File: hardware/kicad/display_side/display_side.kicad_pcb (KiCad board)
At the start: 2 copper layers, 85 x 65 mm, 34 parts, among them J1 RJ45, J2 EPD_FFC_24, J3 UART-DBG, J4 USB-OTG, U1 R-78E3.3-0.5, U2 SN65HVD3082E

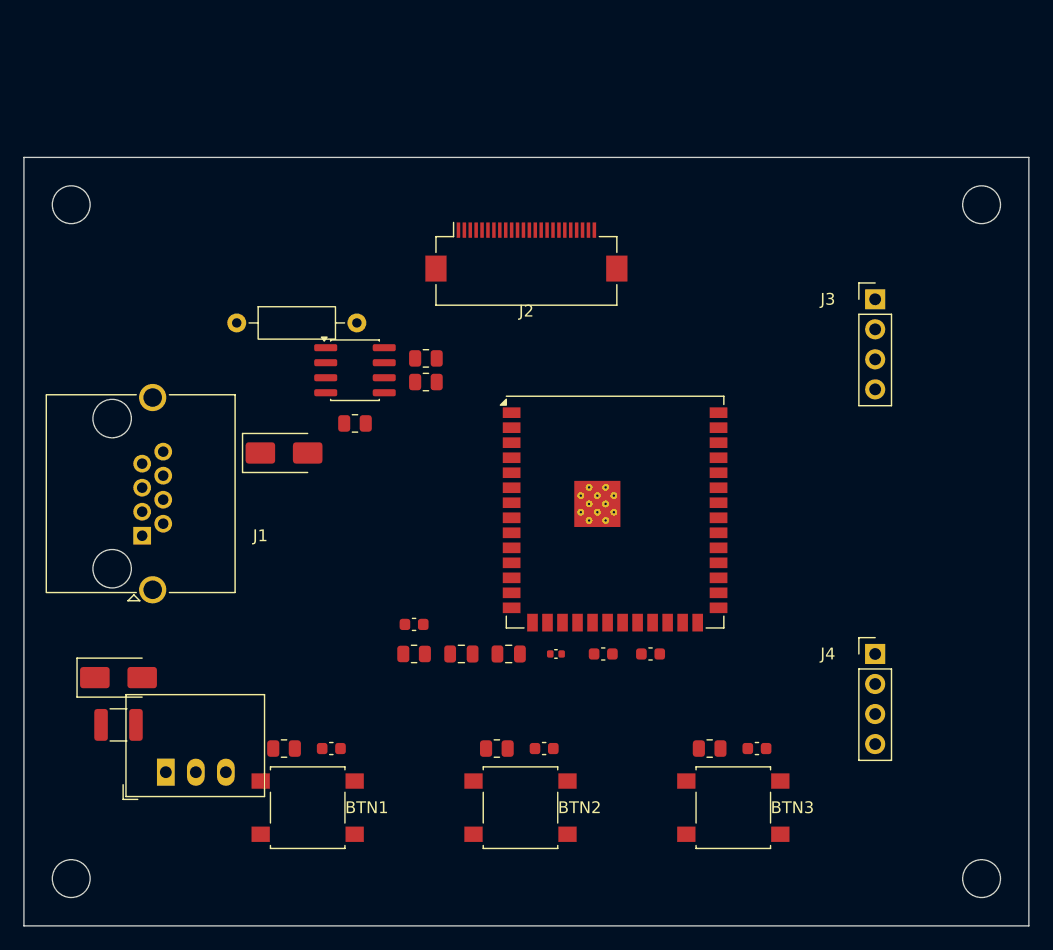
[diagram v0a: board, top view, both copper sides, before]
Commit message: hardware: CP5 iter-2 — net classes + B.Cu ground pour foundation
Addresses Codex iter-1 findings 01-03 partially:

build_pcbs.py:
- _add_ground_zone() helper: B.Cu copper-pour zone with 0.5mm edge
  inset, 0.25mm clearance/min-thickness, thermal-relief PTH connect.
  Called from both build_battery_side() and build_display_side().
- _add_keepout_zone() helper added but not called — both boards use
  ESP32-S3-WROOM-1U (external U.FL), no on-PCB antenna to keep out
  per the iter-18 architectural respin documented at line 282.
- _fill_zones() helper: invokes KiCad's pcbnew Python under wx-app
  context to compute zone fill polygons and persist them. Without
  this step zones are unfilled in renders.

.kicad_pro (both boards):
- _intended_classes_cp4 + _intended_patterns_cp4 promoted into
  active net_settings.classes (with KiCad 10 schema fields) and
  netclass_patterns. The intent docs in cp1_*.md §10.3/§11.3 are
  now enforced by KiCad's clearance checker.

D11 visual inspection iter-2 artifacts:
- hardware/reviews/visual_inspections/cp5-routing-drc/iter2/
  {battery,display}_{top,bottom}.png + MANIFEST.sha256
- packet §D11 visual inspection section with embedded renders +
  sign-off scorecard (F-S-1/F-P-2/F-P-3/SR-1/F-V-1 PASS, F-S-2/F-P-1
  FAIL pending routing, F-P-4 N/A — no antenna keepout needed).

DRC summary at hardware/outputs/{battery_side,display_side}/drc-cp5-iter2.rpt:
- battery: 388 violations (+29 vs CP3 baseline 359 — net-class
  clearance now exposes pre-existing pad-on-pad overlaps in CP3
  placement), 46 schematic parity unchanged.
- display: 94 violations (unchanged from CP4 APPROVED baseline),
  34 parity unchanged.

Q-CP5-1 implicitly answered: build host has no Java Runtime so
Freerouting is unavailable. Iter-3 plan: hand-write critical power
paths (V24/V12) + RS-485 diff pair programmatically.

SEMAPHORE: claude_turn iter-2 → codex_turn iter-3.
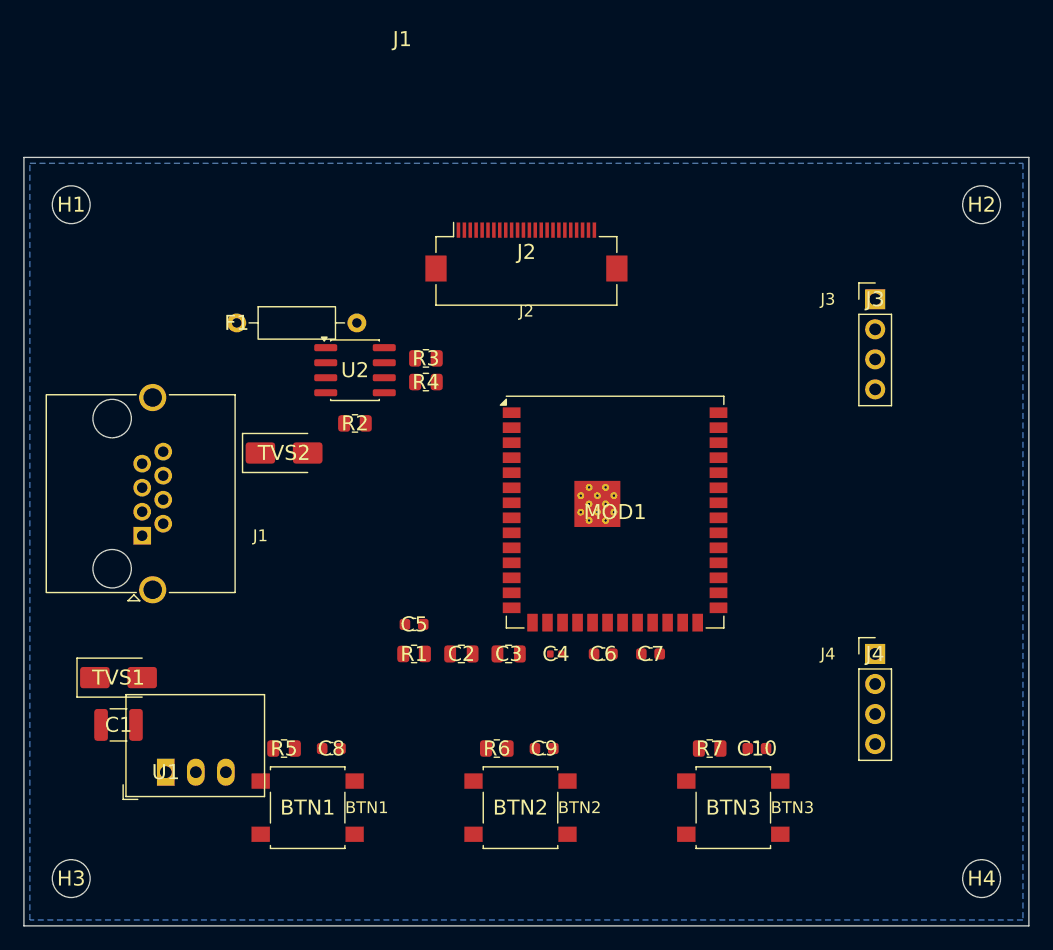
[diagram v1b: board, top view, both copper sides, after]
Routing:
- added copper zone on B.Cu, net GND
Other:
- rule pad_to_mask_clearance: 0.0 -> 0
